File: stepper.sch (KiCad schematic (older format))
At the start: 23 parts, among them U1 L6470H

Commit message: Values
Viable version of schematic. Calculated values and attached footprints.
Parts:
- removed J?: Screw_Terminal_1x02, symbol Screw_Terminal_1x02
- added C1: 10u, Capacitors_THT:CP_Radial_D6.3mm_P2.50mm, symbol CP
- added C10: 0.1, Capacitors_SMD:C_0805, symbol C
- added C4: 100u, Capacitors_THT:CP_Radial_D10.0mm_P3.50mm, symbol CP
- added D1, D2: BZV55C10, Diodes_SMD:D_MiniMELF, symbol D_Zener
- added D6: BZV55C3V6, Diodes_SMD:D_MiniMELF, symbol D_Zener
- added J1: CONN_01X02, Pin_Headers:Pin_Header_Straight_1x02_Pitch2.54mm, symbol CONN_01X02
- added Q1: IRFR5410, TO_SOT_Packages_SMD:TO-252-2, symbol Q_PMOS_GDS
- added R1: 100k, Resistors_SMD:R_0805, symbol R
- added RV1: 200k, Potentiometers:Potentiometer_Trimmer_Bourns_3296P, symbol POT
- C2: renamed from C?; value CP -> 100u; footprint (none) -> Capacitors_THT:CP_Radial_D10.0mm_P3.50mm; Voltage (none) -> 100
- C3: renamed from C?; value C -> 0.22; footprint (none) -> Capacitors_SMD:C_0805; Voltage (none) -> 100
- C5: renamed from C?; value CP -> 10u; footprint (none) -> Capacitors_THT:CP_Radial_D6.3mm_P2.50mm; Voltage (none) -> 25
- C6: renamed from C?; value C -> 0.1; footprint (none) -> Capacitors_SMD:C_0805; Voltage (none) -> 25
- C7: renamed from C?; value C -> 0.1; footprint (none) -> Capacitors_SMD:C_0805; Voltage (none) -> 6.3
- C8: renamed from C?; value C -> 220n; footprint (none) -> Capacitors_SMD:C_0805; Voltage (none) -> 16v
- C9: renamed from C?; value C -> 10n; footprint (none) -> Capacitors_SMD:C_0805; Voltage (none) -> 50v
- D3, D4: renamed from D?; footprint (none) -> LEDs:LED_0805
- D5: renamed from D?; footprint Package_TO_SOT_SMD:SOT-23 -> TO_SOT_Packages_SMD:SOT-23
- J2, J4: renamed from J?; footprint (none) -> Pin_Headers:Pin_Header_Straight_1x02_Pitch2.54mm
- J3: renamed from J?; footprint (none) -> Pin_Headers:Pin_Header_Straight_2x05_Pitch2.54mm
- J5, J6: renamed from J?; footprint (none) -> TerminalBlock:TerminalBlock_bornier-2_P5.08mm
- R2: renamed from R?; value R -> 100; footprint (none) -> Resistors_SMD:R_0805
- R3, R4: renamed from R?; value R -> 510; footprint (none) -> Resistors_SMD:R_0805
- R5: renamed from R?; value R -> 31k6; footprint (none) -> Resistors_SMD:R_0805
- R6: renamed from R?; value R -> 8k2; footprint (none) -> Resistors_SMD:R_0805
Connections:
- net GND: now also C1.2, C10.1, C4.2, D6.2 (A), J1.2 (P2), R1.2
- net SW: no longer C7.1
- net VCC: now also D5.1 (A), C1.1, D2.1 (K), Q1.3 (S); no longer D5.1 (A)
- net VDD: now also C4.1
- net at C8.1, U1.11 (VBOOT): now also D5.2 (K); no longer D5.2 (K)
- net at R2.1, U1.4 (SW): now also C7.1
- net at R6.2, U1.5 (ADCIN): now also C10.2, D6.1 (K), RV1.1, RV1.2; no longer R5.1
- new net: R5.1, RV1.3
- new net: D1.1 (K), Q1.1 (G), R1.1
- new net: J1.1 (P1), Q1.2 (D)
- new net: D1.2 (A), D2.2 (A)
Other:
- moved on the sheet: C2, C3, C5, C6, J4, J5, J6, R2, R5, R6

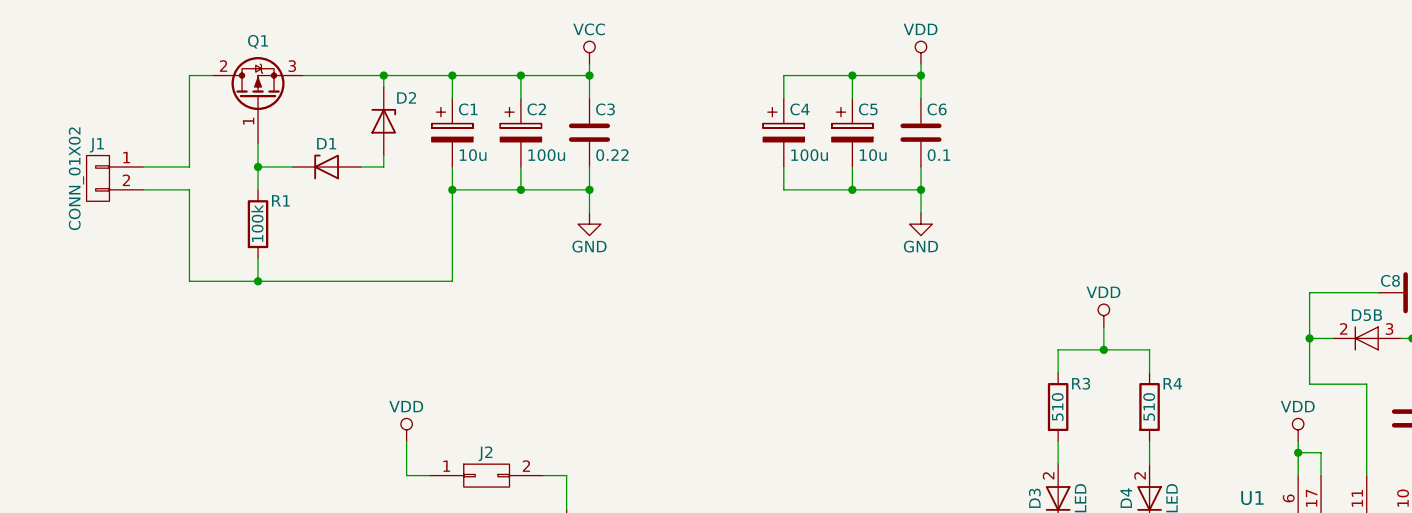
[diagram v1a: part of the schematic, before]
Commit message: Caps
Some changes in VCC filtration capcitors.
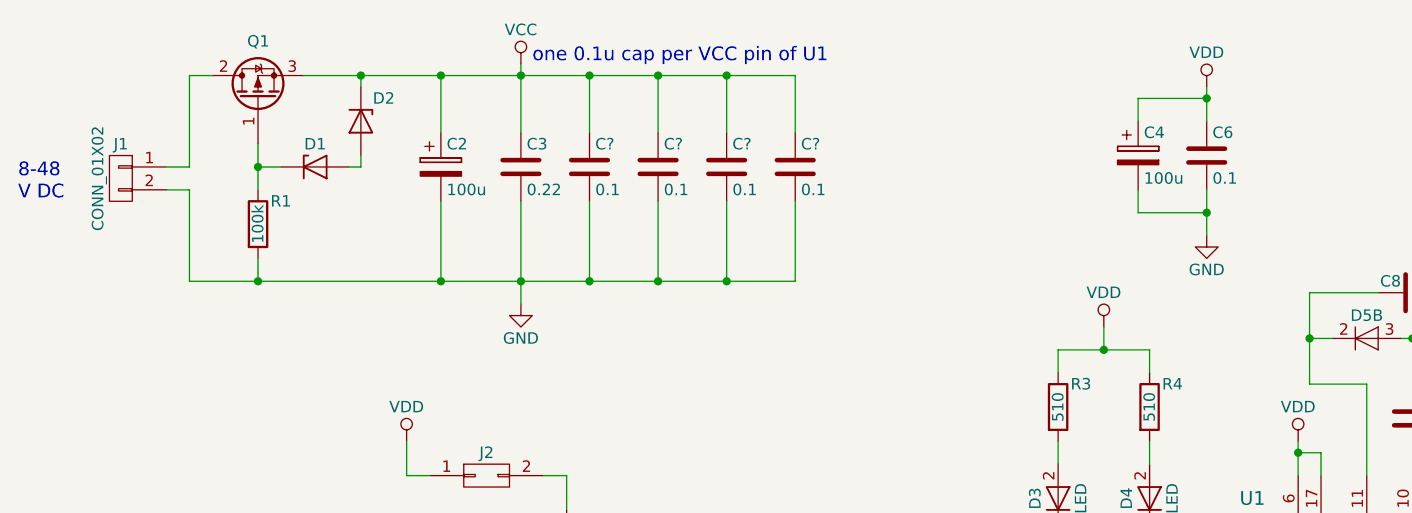
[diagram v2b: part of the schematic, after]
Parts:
- removed C1, C5: 10u, Capacitors_THT:CP_Radial_D6.3mm_P2.50mm, symbol CP
- added C? (x4): 0.1, Capacitors_SMD:C_0805, symbol C
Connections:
- net GND: now also C?.2, C?.2, C?.2, C?.2
- net VCC: now also C?.1, C?.1, C?.1, C?.1
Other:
- note added: "8-48 \nV DC"
- note added: "one 0.1u cap per VCC pin of U1"
- moved on the sheet: C2, C3, C4, C6, D1, D2, J1

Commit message: PCB
Routed PCB
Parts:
- added C10: 10, Capacitors_SMD:C_0805, symbol C
- RV1: footprint Potentiometers:Potentiometer_Trimmer_Bourns_3296P -> Potentiometers:Potentiometer_Trimmer_Bourns_3266W
- gave numbers to parts that had none: 4
- renumbered C2 to C1, C8 to C11, C9 to C12, C10 to C13, C3 to C2, C4 to C8, C6 to C9
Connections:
- net GND: now also C10.2
- net VDD: now also C10.1
- net at U1.1 (OUT1A): now also J5.2; no longer J5.1
- net at U1.28 (OUT2A): now also J5.1; no longer J5.2
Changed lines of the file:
@@
 $EndComp
 $Comp
-L C C9
+L C C12
 U 1 1 5A75FE3B
 P 7100 2650
-F 0 "C9" H 7125 2750 50  0000 L CNN
+F 0 "C12" H 7125 2750 50  0000 L CNN
 F 1 "10n" H 7125 2550 50  0000 L CNN
 F 2 "Capacitors_SMD:C_0805" H 7138 2500 50  0001 C CNN
@@
 $EndComp
 $Comp
-L C C8
+L C C11
 U 1 1 5A7600B1
 P 7100 2100
-F 0 "C8" V 7150 2150 50  0000 L CNN
+F 0 "C11" V 7150 2150 50  0000 L CNN
 F 1 "220n" V 7150 1850 50  0000 L CNN
 F 2 "Capacitors_SMD:C_0805" H 7138 1950 50  0001 C CNN
@@
 $EndComp
 $Comp
-L C C6
+L C C9
 U 1 1 5A760BD2
 P 6200 1500
-F 0 "C6" H 6225 1600 50  0000 L CNN
+F 0 "C9" H 6225 1600 50  0000 L CNN
 F 1 "0.1" H 6225 1400 50  0000 L CNN
 F 2 "Capacitors_SMD:C_0805" H 6238 1350 50  0001 C CNN
@@
 $EndComp
 $Comp
-L C C3
+L C C2
 U 1 1 5A76170E
 P 3200 1550
-F 0 "C3" H 3225 1650 50  0000 L CNN
+F 0 "C2" H 3225 1650 50  0000 L CNN
 F 1 "0.22" H 3225 1450 50  0000 L CNN
 F 2 "Capacitors_SMD:C_0805" H 3238 1400 50  0001 C CNN
@@
 $EndComp
 $Comp
-L CP C2
+L CP C1
 U 1 1 5A761714
 P 2850 1550
-F 0 "C2" H 2875 1650 50  0000 L CNN
+F 0 "C1" H 2875 1650 50  0000 L CNN
 F 1 "100u" H 2875 1450 50  0000 L CNN
 F 2 "Capacitors_THT:CP_Radial_D10.0mm_P3.50mm" H 2888 1400 50  0001 C CNN
@@
 F 3 "" H 9275 3650 50  0001 C CNN
 	1    9300 3650
-	-1   0    0    -1
+	-1   0    0    1
 $EndComp
 $Comp
@@
 F 0 "RV1" V 8075 2800 50  0000 C CNN
 F 1 "200k" V 8150 2800 50  0000 C CNN
-F 2 "Potentiometers:Potentiometer_Trimmer_Bourns_3296P" H 8250 2800 50  0001 C CNN
+F 2 "Potentiometers:Potentiometer_Trimmer_Bourns_3266W" H 8250 2800 50  0001 C CNN
 F 3 "" H 8250 2800 50  0001 C CNN
 	1    8250 2800
@@
 $EndComp
 $Comp
-L C C10
+L C C13
 U 1 1 5AA2E94E
 P 8700 3050
-F 0 "C10" V 8600 2850 50  0000 L CNN
+F 0 "C13" V 8600 2850 50  0000 L CNN
 F 1 "0.1" V 8600 3150 50  0000 L CNN
 F 2 "Capacitors_SMD:C_0805" H 8738 2900 50  0001 C CNN
@@
 $EndComp
 $Comp
-L CP C4
+L CP C8
 U 1 1 5AA2EF35
 P 5900 1500
-F 0 "C4" H 5925 1600 50  0000 L CNN
+F 0 "C8" H 5925 1600 50  0000 L CNN
 F 1 "100u" H 5925 1400 50  0000 L CNN
 F 2 "Capacitors_THT:CP_Radial_D10.0mm_P3.50mm" H 5938 1350 50  0001 C CNN
@@
 	6200 1200 6200 1350
 Wire Wire Line
-	5900 1250 6200 1250
+	5900 1250 6500 1250
 Connection ~ 6200 1250
 Wire Wire Line
 	6200 1650 6200 1850
 Wire Wire Line
-	5900 1750 6200 1750
+	5900 1750 6500 1750
 Connection ~ 6200 1750
 Wire Wire Line
@@
 Wire Wire Line
 	8950 2800 8850 2800
-Wire Wire Line
-	9100 3550 7900 3550
-Wire Wire Line
-	9100 3750 7900 3750
 Wire Wire Line
 	9100 4150 7900 4150
@@
 8-48 \nV DC
 $Comp
-L C C?
+L C C3
 U 1 1 5AA57D26
 P 3500 1550
-F 0 "C?" H 3525 1650 50  0000 L CNN
+F 0 "C3" H 3525 1650 50  0000 L CNN
 F 1 "0.1" H 3525 1450 50  0000 L CNN
 F 2 "Capacitors_SMD:C_0805" H 3538 1400 50  0001 C CNN
@@
 $EndComp
 $Comp
-L C C?
+L C C4
 U 1 1 5AA57DCB
 P 3800 1550
-F 0 "C?" H 3825 1650 50  0000 L CNN
+F 0 "C4" H 3825 1650 50  0000 L CNN
 F 1 "0.1" H 3825 1450 50  0000 L CNN
 F 2 "Capacitors_SMD:C_0805" H 3838 1400 50  0001 C CNN
@@
 $EndComp
 $Comp
-L C C?
+L C C5
 U 1 1 5AA57E47
 P 4100 1550
-F 0 "C?" H 4125 1650 50  0000 L CNN
+F 0 "C5" H 4125 1650 50  0000 L CNN
 F 1 "0.1" H 4125 1450 50  0000 L CNN
 F 2 "Capacitors_SMD:C_0805" H 4138 1400 50  0001 C CNN
@@
 $EndComp
 $Comp
-L C C?
+L C C6
 U 1 1 5AA57EC4
 P 4400 1550
-F 0 "C?" H 4425 1650 50  0000 L CNN
+F 0 "C6" H 4425 1650 50  0000 L CNN
 F 1 "0.1" H 4425 1450 50  0000 L CNN
 F 2 "Capacitors_SMD:C_0805" H 4438 1400 50  0001 C CNN
@@
 Text Notes 3250 1100 0    60   ~ 0
 one 0.1u cap per VCC pin of U1
+Wire Wire Line
+	9100 3550 7900 3550
+Wire Wire Line
+	7900 3750 9100 3750
+$Comp
+L C C10
+U 1 1 5AA5BF0E
+P 6500 1500
+F 0 "C10" H 6525 1600 50  0000 L CNN
+F 1 "10" H 6525 1400 50  0000 L CNN
+F 2 "Capacitors_SMD:C_0805" H 6538 1350 50  0001 C CNN
+F 3 "" H 6500 1500 50  0001 C CNN
+F 4 "25" H 6500 1500 60  0001 C CNN "Voltage"
+	1    6500 1500
+	1    0    0    -1
+$EndComp
+Wire Wire Line
+	6500 1250 6500 1350
+Wire Wire Line
+	6500 1750 6500 1650
 $EndSCHEMATC
